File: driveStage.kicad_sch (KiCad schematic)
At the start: 57 parts, among them J1 MOD_IN, Q1 SQJA70EP-T1, SW1 SW_DIP_x03, U1 LTC6655BHLS8-4.096, U2 MAX5719xSD, U3 ADA4898-1YRDZ, U4 ADA4898-1YRDZ, U5 RS8552, U6 ADA4898-1YRDZ

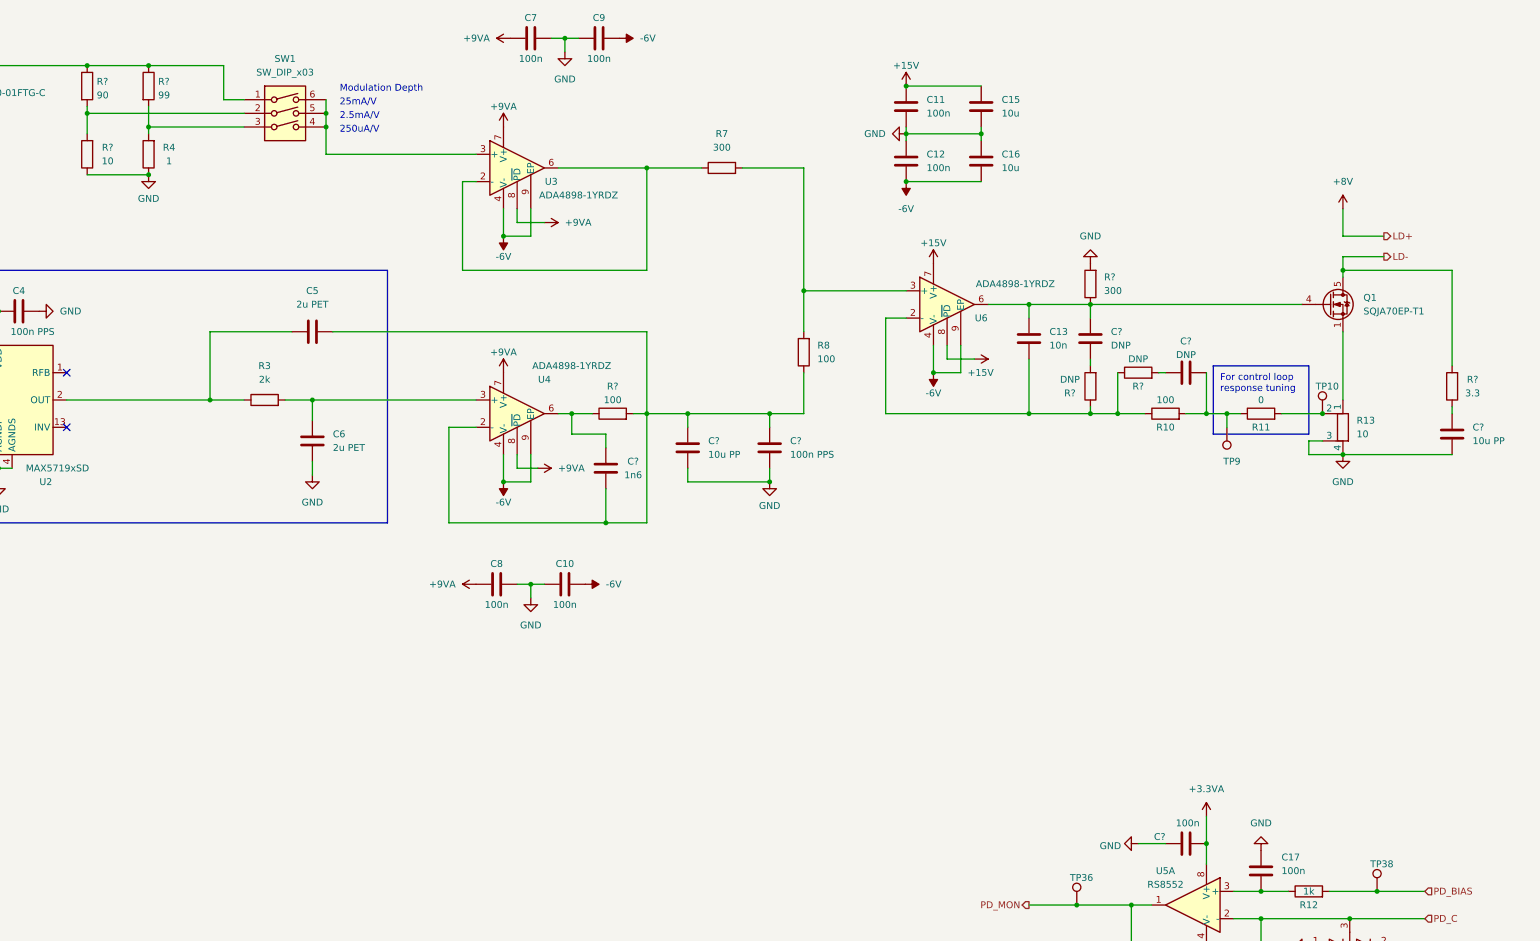
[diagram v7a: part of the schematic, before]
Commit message: change damper
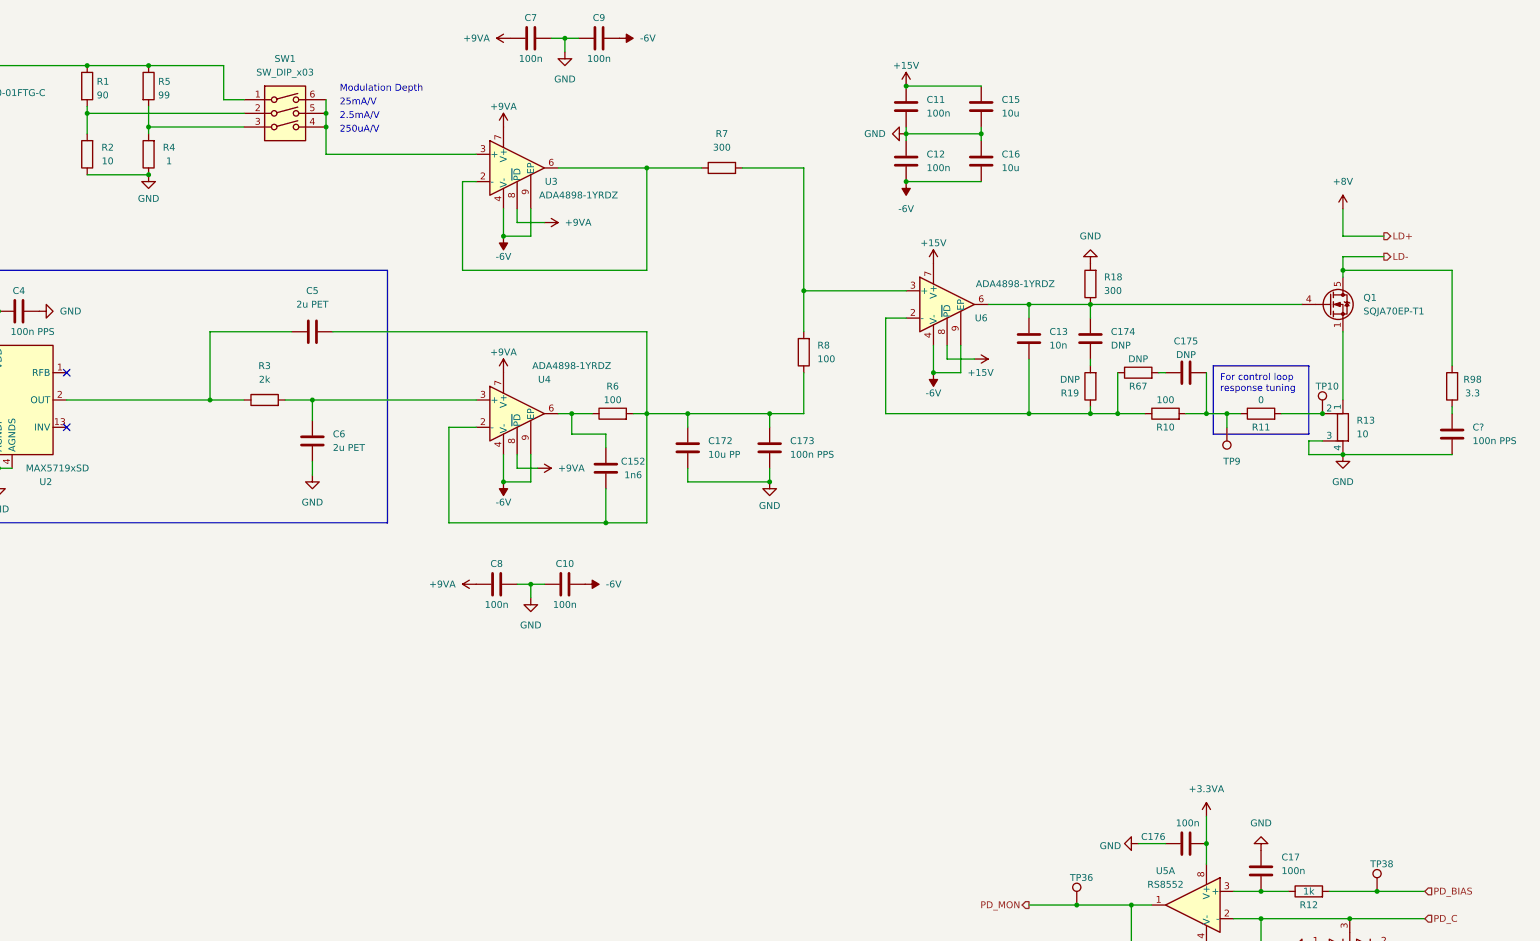
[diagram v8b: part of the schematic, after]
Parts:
- removed C?: 10u PP, Capacitor_SMD:C_1812_4532Metric, symbol Device:C
- added C?: 100n PPS, Capacitor_SMD:C_1210_3225Metric, symbol Device:C
- gave numbers to parts that had none: 14
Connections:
- net GND: now also C?.2
- net at R98.1: now also C?.1
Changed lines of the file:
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@@
   (symbol (lib_id "Device:R") (at 320.04 111.76 180) (unit 1)
     (in_bom yes) (on_board yes)
-    (property "Reference" "R?" (id 0) (at 316.23 113.03 0))
+    (property "Reference" "R19" (id 0) (at 316.23 113.03 0))
     (property "Value" "DNP" (id 1) (at 316.23 110.49 0))
     (property "Footprint" "Resistor_SMD:R_0603_1608Metric" (id 2) (at 321.818 111.76 90)
@@
   (symbol (lib_id "Device:R") (at 320.04 92.71 180) (unit 1)
     (in_bom yes) (on_board yes) (fields_autoplaced)
-    (property "Reference" "R?" (id 0) (at 322.58 91.4399 0)
+    (property "Reference" "R18" (id 0) (at 322.58 91.4399 0)
       (effects (font (size 1.27 1.27)) (justify right))
     )
@@
   (symbol (lib_id "power:GND") (at 328.93 196.85 270) (unit 1)
     (in_bom yes) (on_board yes) (fields_autoplaced)
-    (property "Reference" "#PWR?" (id 0) (at 322.58 196.85 0)
+    (property "Reference" "#PWR0130" (id 0) (at 322.58 196.85 0)
       (effects (font (size 1.27 1.27)) hide)
     )
@@
   (symbol (lib_id "Device:C") (at 320.04 102.87 0) (unit 1)
     (in_bom yes) (on_board yes) (fields_autoplaced)
-    (property "Reference" "C?" (id 0) (at 323.85 101.5999 0)
+    (property "Reference" "C174" (id 0) (at 323.85 101.5999 0)
       (effects (font (size 1.27 1.27)) (justify left))
     )
@@
   (symbol (lib_id "Device:R") (at 387.35 111.76 180) (unit 1)
     (in_bom yes) (on_board yes)
-    (property "Reference" "R?" (id 0) (at 391.16 110.49 0))
+    (property "Reference" "R98" (id 0) (at 391.16 110.49 0))
     (property "Value" "3.3" (id 1) (at 391.16 113.03 0))
     (property "Footprint" "Resistor_SMD:R_0603_1608Metric" (id 2) (at 389.128 111.76 90)
@@
     (pin "1")
   )
+  (symbol (lib_id "Device:C") (at 387.35 120.65 0) (unit 1)
+    (in_bom yes) (on_board yes) (fields_autoplaced)
+    (property "Reference" "C?" (id 0) (at 391.16 119.3799 0)
+      (effects (font (size 1.27 1.27)) (justify left))
+    )
+    (property "Value" "100n PPS" (id 1) (at 391.16 121.9199 0)
+      (effects (font (size 1.27 1.27)) (justify left))
+    )
+    (property "Footprint" "Capacitor_SMD:C_1210_3225Metric" (id 2) (at 388.3152 124.46 0)
+      (effects (font (size 1.27 1.27)) hide)
+    )
+    (property "Datasheet" "~" (id 3) (at 387.35 120.65 0)
+      (effects (font (size 1.27 1.27)) hide)
+    )
+    (property "MFR_PN" "ECH-U1C104JX5" (id 4) (at 387.35 120.65 0)
+      (effects (font (size 1.27 1.27)) hide)
+    )
+    (pin "1")
+    (pin "2")
+  )
   (symbol (lib_id "Device:R") (at 266.7 105.41 180) (unit 1)
     (in_bom yes) (on_board yes) (fields_autoplaced)
@@
   (symbol (lib_id "Device:R") (at 133.35 68.58 180) (unit 1)
     (in_bom yes) (on_board yes)
-    (property "Reference" "R?" (id 0) (at 137.16 67.31 0))
+    (property "Reference" "R2" (id 0) (at 137.16 67.31 0))
     (property "Value" "10" (id 1) (at 137.16 69.85 0))
     (property "Footprint" "Resistor_SMD:R_0603_1608Metric" (id 2) (at 135.128 68.58 90)
@@
   (symbol (lib_id "power:GND") (at 320.04 88.9 180) (unit 1)
     (in_bom yes) (on_board yes) (fields_autoplaced)
-    (property "Reference" "#PWR?" (id 0) (at 320.04 82.55 0)
+    (property "Reference" "#PWR035" (id 0) (at 320.04 82.55 0)
       (effects (font (size 1.27 1.27)) hide)
     )
@@
   (symbol (lib_id "Device:C") (at 245.11 123.19 0) (unit 1)
     (in_bom yes) (on_board yes) (fields_autoplaced)
-    (property "Reference" "C?" (id 0) (at 248.92 121.9199 0)
+    (property "Reference" "C172" (id 0) (at 248.92 121.9199 0)
       (effects (font (size 1.27 1.27)) (justify left))
     )
@@
     (pin "2")
   )
-  (symbol (lib_id "Device:C") (at 387.35 120.65 0) (unit 1)
-    (in_bom yes) (on_board yes) (fields_autoplaced)
-    (property "Reference" "C?" (id 0) (at 391.16 119.3799 0)
-      (effects (font (size 1.27 1.27)) (justify left))
-    )
-    (property "Value" "10u PP" (id 1) (at 391.16 121.9199 0)
-      (effects (font (size 1.27 1.27)) (justify left))
-    )
-    (property "Footprint" "Capacitor_SMD:C_1812_4532Metric" (id 2) (at 388.3152 124.46 0)
-      (effects (font (size 1.27 1.27)) hide)
-    )
-    (property "Datasheet" "~" (id 3) (at 387.35 120.65 0)
-      (effects (font (size 1.27 1.27)) hide)
-    )
-    (property "MFR_PN" "16MU106MC44532" (id 4) (at 387.35 120.65 0)
-      (effects (font (size 1.27 1.27)) hide)
-    )
-    (pin "1")
-    (pin "2")
-  )
   (symbol (lib_id "Device:C") (at 229.87 127 180) (unit 1)
     (in_bom yes) (on_board yes)
-    (property "Reference" "C?" (id 0) (at 234.95 125.73 0))
+    (property "Reference" "C152" (id 0) (at 234.95 125.73 0))
     (property "Value" "1n6" (id 1) (at 234.95 128.27 0))
     (property "Footprint" "Capacitor_SMD:C_0603_1608Metric" (id 2) (at 228.9048 123.19 0)
@@
   (symbol (lib_id "Device:R") (at 144.78 55.88 0) (unit 1)
     (in_bom yes) (on_board yes) (fields_autoplaced)
-    (property "Reference" "R?" (id 0) (at 146.558 55.0453 0)
+    (property "Reference" "R5" (id 0) (at 146.558 55.0453 0)
       (effects (font (size 1.27 1.27)) (justify left))
     )
@@
   (symbol (lib_id "Device:C") (at 337.82 109.22 90) (unit 1)
     (in_bom yes) (on_board yes) (fields_autoplaced)
-    (property "Reference" "C?" (id 0) (at 337.82 103.3612 90))
+    (property "Reference" "C175" (id 0) (at 337.82 103.3612 90))
     (property "Value" "DNP" (id 1) (at 337.82 105.8981 90))
     (property "Footprint" "Capacitor_SMD:C_0603_1608Metric" (id 2) (at 341.63 108.2548 0)
@@
   (symbol (lib_id "Device:R") (at 328.93 109.22 90) (unit 1)
     (in_bom yes) (on_board yes)
-    (property "Reference" "R?" (id 0) (at 328.93 111.76 90))
+    (property "Reference" "R67" (id 0) (at 328.93 111.76 90))
     (property "Value" "DNP" (id 1) (at 328.93 106.68 90))
     (property "Footprint" "Resistor_SMD:R_0603_1608Metric" (id 2) (at 328.93 110.998 90)
@@
   (symbol (lib_id "power:GND") (at 144.78 72.39 0) (unit 1)
     (in_bom yes) (on_board yes) (fields_autoplaced)
-    (property "Reference" "#PWR?" (id 0) (at 144.78 78.74 0)
+    (property "Reference" "#PWR012" (id 0) (at 144.78 78.74 0)
       (effects (font (size 1.27 1.27)) hide)
     )
@@
   (symbol (lib_id "Device:C") (at 337.82 196.85 90) (unit 1)
     (in_bom yes) (on_board yes)
-    (property "Reference" "C?" (id 0) (at 334.01 195.58 90)
+    (property "Reference" "C176" (id 0) (at 334.01 195.58 90)
       (effects (font (size 1.27 1.27)) (justify left))
     )
@@
   (symbol (lib_id "Device:R") (at 133.35 55.88 0) (unit 1)
     (in_bom yes) (on_board yes) (fields_autoplaced)
-    (property "Reference" "R?" (id 0) (at 135.128 55.0453 0)
+    (property "Reference" "R1" (id 0) (at 135.128 55.0453 0)
       (effects (font (size 1.27 1.27)) (justify left))
     )
@@
   (symbol (lib_id "power:GND") (at 260.35 129.54 0) (unit 1)
     (in_bom yes) (on_board yes) (fields_autoplaced)
-    (property "Reference" "#PWR?" (id 0) (at 260.35 135.89 0)
+    (property "Reference" "#PWR034" (id 0) (at 260.35 135.89 0)
       (effects (font (size 1.27 1.27)) hide)
     )
@@
   (symbol (lib_id "Device:R") (at 231.14 116.84 90) (unit 1)
     (in_bom yes) (on_board yes)
-    (property "Reference" "R?" (id 0) (at 231.14 111.76 90))
+    (property "Reference" "R6" (id 0) (at 231.14 111.76 90))
     (property "Value" "100" (id 1) (at 231.14 114.3 90))
     (property "Footprint" "Resistor_SMD:R_0603_1608Metric" (id 2) (at 231.14 118.618 90)
@@
   (symbol (lib_id "Device:C") (at 260.35 123.19 0) (unit 1)
     (in_bom yes) (on_board yes) (fields_autoplaced)
-    (property "Reference" "C?" (id 0) (at 264.16 121.9199 0)
-      (effects (font (size 1.27 1.27)) (justify left))
-    )
+    (property "Reference" "C173" (id 0) (at 264.16 121.9199 0)
+      (effects (font (size 1.27 1.27)) (justify left))
+    )
